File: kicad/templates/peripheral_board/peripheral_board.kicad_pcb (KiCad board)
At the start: 2 copper layers, 203.2 x 97.8 mm, 6 parts, among them J1 peripheral_addr_bus_connector, J2 peripheral_aux_connector, J3 peripheral_membank_connector

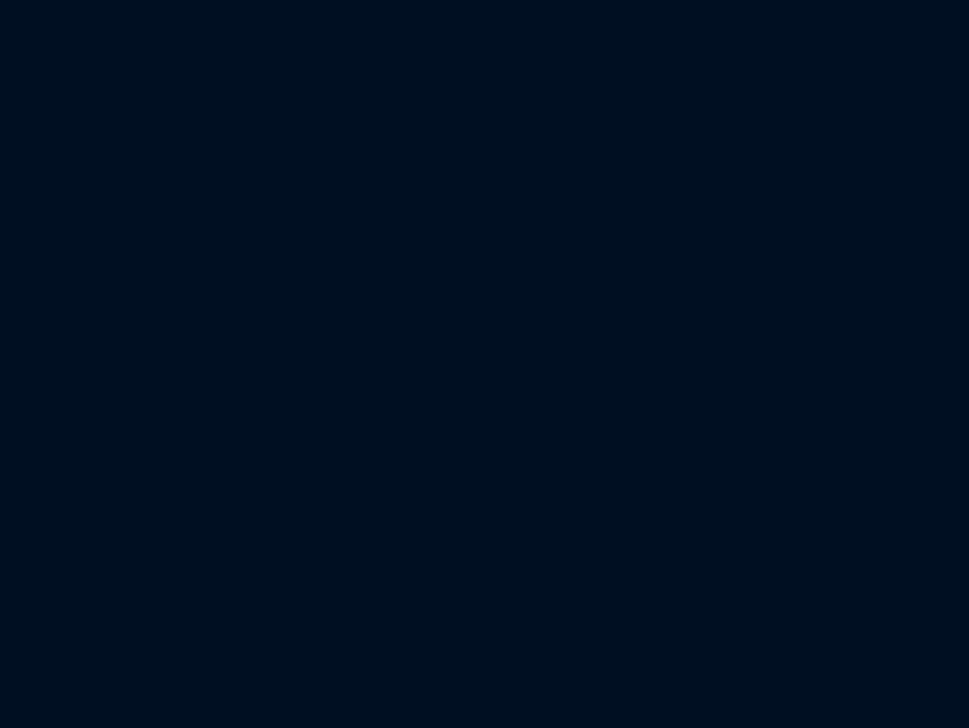
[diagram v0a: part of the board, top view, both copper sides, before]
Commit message: Add resistor, capacitor and test points to periperal template.
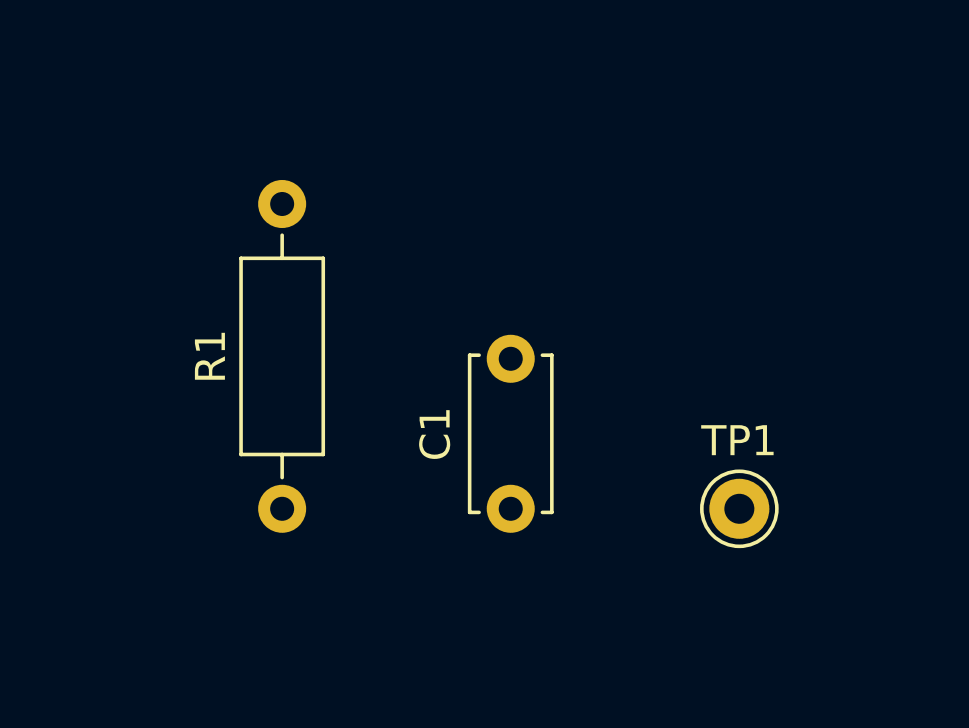
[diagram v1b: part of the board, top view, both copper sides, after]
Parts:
- added C1: C, Capacitor_THT:C_Disc_D5.0mm_W2.5mm_P5.00mm, F.Cu at (152.4, 96.5)
- added R1: R_US, Resistor_THT:R_Axial_DIN0207_L6.3mm_D2.5mm_P10.16mm_Horizontal, F.Cu at (144.8, 96.5)
- added TP1: TestPoint, Connector_Pin:Pin_D1.0mm_L10.0mm, F.Cu at (160.0, 96.5)
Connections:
- J2 pad 10: unconnected-(J2-RFM-Pad10) -> /RFM
- J2 pad 12: unconnected-(J2-WTM-Pad12) -> /WTM
- J2 pad 14: unconnected-(J2-RST-Pad14) -> /RESET
- J2 pad 6: unconnected-(J2-DCLK-Pad6) -> /DATA_CLK
- J2 pad 8: unconnected-(J2-CCLK-Pad8) -> /CTL_CLK
